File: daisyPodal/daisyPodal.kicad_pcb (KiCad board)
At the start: 2 copper layers, 76 x 82 mm, 50 parts, among them J1 Guitar in, J2 fsw pin 1, J3 fsw pin 2, J4 fsw pin 4, J5 fsw pin 5, J6 fsw pin 6, J7 Left out, J8 Right out, J9 fsw pin 3, SW1 Switch 1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

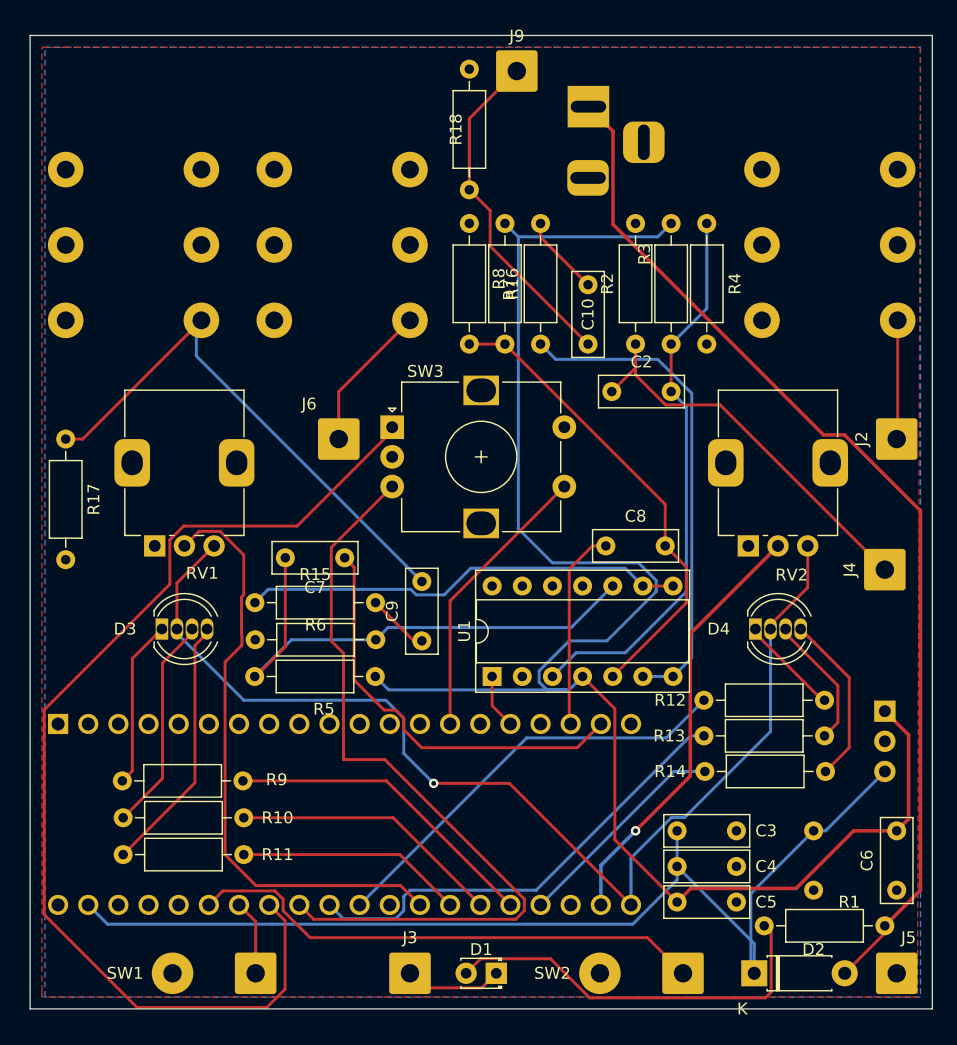
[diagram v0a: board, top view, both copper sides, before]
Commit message: Terminate unused op-amp
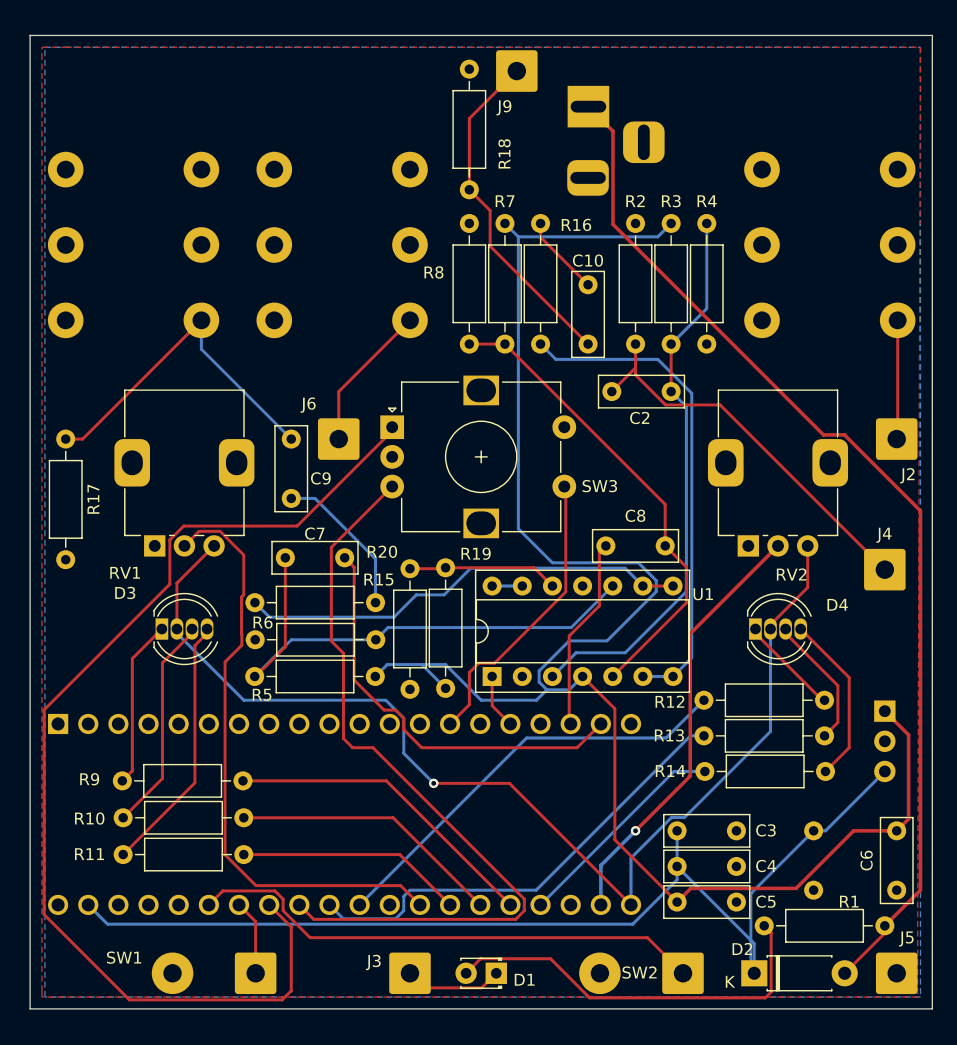
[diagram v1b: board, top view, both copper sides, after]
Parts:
- added R19: 1M, Resistor_THT:R_Axial_DIN0207_L6.3mm_D2.5mm_P10.16mm_Horizontal, F.Cu at (134.0, 107.0)
- added R20: 1M, Resistor_THT:R_Axial_DIN0207_L6.3mm_D2.5mm_P10.16mm_Horizontal, F.Cu at (131.0, 96.9)
- moved C9 16.3 mm to (121.0, 91.0)
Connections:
- U1 pad 12: (no net) -> Net-(U1D-+)
- U1 pad 13: (no net) -> Net-(U1D--)
- U1 pad 14: (no net) -> Net-(U1D--)
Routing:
- net Net-(C9-Pad2): track 45.9 -> 29.1 mm
- net Net-(U1D-+): track 0.00 -> 12.7 mm
- net Net-(C9-Pad1): track 5.24 -> 12.9 mm
- net Net-(U1D--): track 0.00 -> 2.54 mm
- net +5V: track 143.3 -> 145.8 mm
- net Net-(A1-SAI2_SD_B): track 66.4 -> 65.3 mm
- net /ENC_CLICK: track 24.0 -> 24.9 mm
- net /Left out: track 17.0 -> 16.3 mm
- net Net-(U1C--): track 37.4 -> 38.1 mm

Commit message: Add low pass filters at 22kHz on outputs
Following advice from Daisy forum discussion on Seed rev 7 noise.
Possible to jumper over these if not desired.
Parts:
- added C11: 2.2nF, Capacitor_THT:C_Rect_L7.0mm_W2.5mm_P5.00mm, F.Cu at (152.5, 91.8)
- added C12: 2.2nF, Capacitor_THT:C_Rect_L7.0mm_W2.5mm_P5.00mm, F.Cu at (102.0, 103.0)
- added R21: 3.3K, Resistor_THT:R_Axial_DIN0207_L6.3mm_D2.5mm_P10.16mm_Horizontal, F.Cu at (171.0, 106.1)
- added R22: 3.3K, Resistor_THT:R_Axial_DIN0207_L6.3mm_D2.5mm_P10.16mm_Horizontal, F.Cu at (112.1, 107.0)
- moved J4 5.04 mm to (171.6, 92.0)
- moved R17 1.16 mm to (102.0, 84.8)
- moved J2 0.49 mm to (171.5, 86.0)
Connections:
- C7 pad 1: /Right out -> Net-(C12-Pad2)
- C8 pad 1: /Left out -> Net-(C11-Pad2)
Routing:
- net Net-(C11-Pad2): track 0.00 -> 37.7 mm, vias 0 -> 1
- net Net-(C12-Pad2): track 0.00 -> 34.3 mm
- net /Left out: track 16.3 -> 33.7 mm
- net GND: track 0.00 -> 8.93 mm
- net Net-(BT1-+): track 88.3 -> 94.2 mm
- net /Right out: track 35.2 -> 38.4 mm, vias 0 -> 1
- net Net-(J4-Pin_1): track 35.2 -> 33.8 mm
- net Net-(A1-SAI2_SD_A): track 90.9 -> 91.5 mm

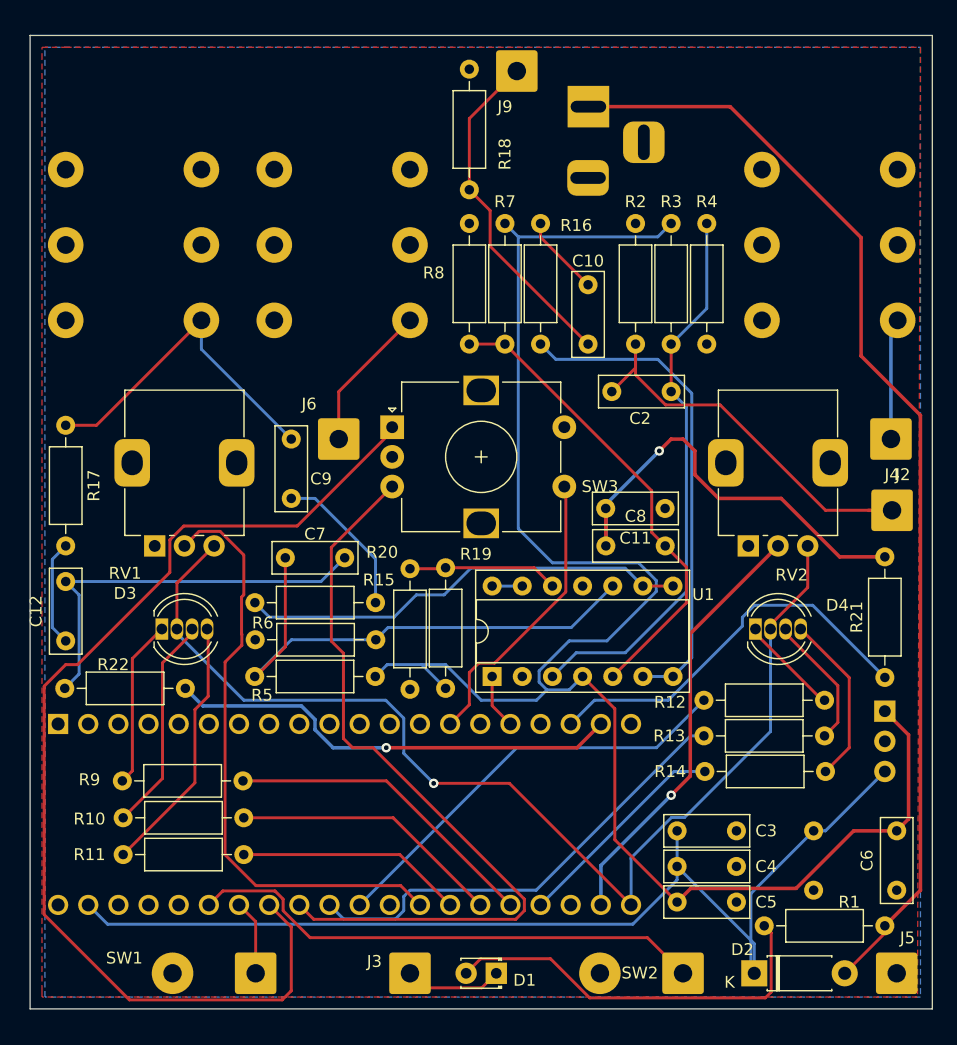
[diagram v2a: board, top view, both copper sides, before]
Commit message: Tidy up various overlaps
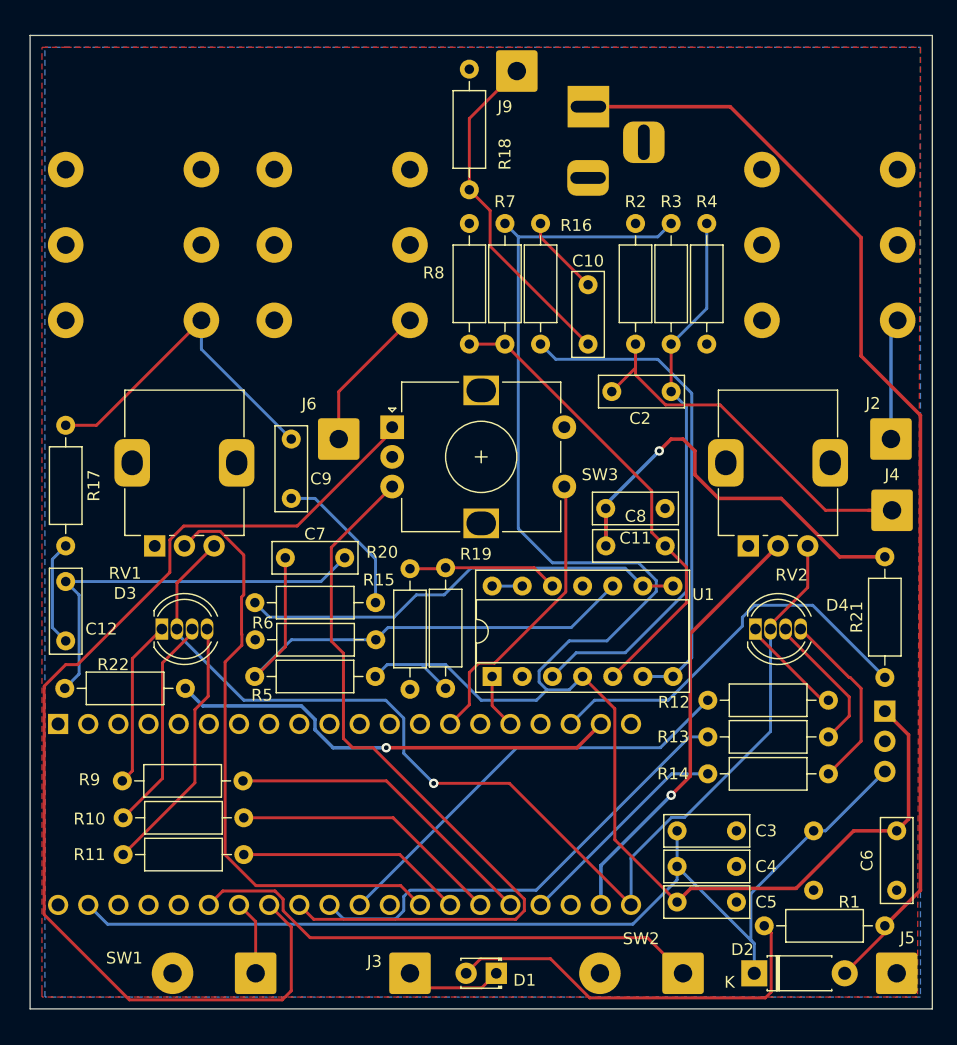
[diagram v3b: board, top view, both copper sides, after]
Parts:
- moved R13 0.34 mm to (156.1, 111.1)
- moved R12 0.33 mm to (156.1, 108.0)
- moved R14 0.32 mm to (156.1, 114.2)
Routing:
- net /VCC: track 90.0 -> 87.9 mm
- net Net-(D4-BK): track 14.5 -> 15.5 mm
- net Net-(D4-GK): track 11.3 -> 12.0 mm
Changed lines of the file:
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@@
   )
   (footprint "Resistor_THT:R_Axial_DIN0207_L6.3mm_D2.5mm_P10.16mm_Horizontal" (layer "F.Cu")
-    (at 155.76 111)
+    (at 156.087773 111.085472)
     (descr "Resistor, Axial_DIN0207 series, Axial, Horizontal, pin pitch=10.16mm, 0.25W = 1/4W, length*diameter=6.3*2.5mm^2, http://cdn-reichelt.de/documents/datenblatt/B400/1_4W%23YAG.pdf")
     (tags "Resistor Axial_DIN0207 series Axial Horizontal pin pitch 10.16mm 0.25W = 1/4W length 6.3mm diameter 2.5mm")
@@
     (property "ki_keywords" "connector")
     (attr exclude_from_pos_files)
-    (fp_text reference "J2" (at -3 1 180) (layer "F.SilkS")
+    (fp_text reference "J2" (at 2.995907 -1.514377 180) (layer "F.SilkS")
         (effects (font (size 1 1) (thickness 0.15)))
     )
@@
   )
   (footprint "Resistor_THT:R_Axial_DIN0207_L6.3mm_D2.5mm_P10.16mm_Horizontal" (layer "F.Cu")
-    (at 155.84 114)
+    (at 156.087773 114.197775)
     (descr "Resistor, Axial_DIN0207 series, Axial, Horizontal, pin pitch=10.16mm, 0.25W = 1/4W, length*diameter=6.3*2.5mm^2, http://cdn-reichelt.de/documents/datenblatt/B400/1_4W%23YAG.pdf")
     (tags "Resistor Axial_DIN0207 series Axial Horizontal pin pitch 10.16mm 0.25W = 1/4W length 6.3mm diameter 2.5mm")
@@
   )
   (footprint "Resistor_THT:R_Axial_DIN0207_L6.3mm_D2.5mm_P10.16mm_Horizontal" (layer "F.Cu")
-    (at 155.76 108)
+    (at 156.087773 108)
     (descr "Resistor, Axial_DIN0207 series, Axial, Horizontal, pin pitch=10.16mm, 0.25W = 1/4W, length*diameter=6.3*2.5mm^2, http://cdn-reichelt.de/documents/datenblatt/B400/1_4W%23YAG.pdf")
     (tags "Resistor Axial_DIN0207 series Axial Horizontal pin pitch 10.16mm 0.25W = 1/4W length 6.3mm diameter 2.5mm")
@@
     (property "ki_keywords" "rotary switch encoder switch push button")
     (attr through_hole)
-    (fp_text reference "SW3" (at 17.5 5) (layer "F.SilkS")
+    (fp_text reference "SW3" (at 17.5 4) (layer "F.SilkS")
         (effects (font (size 1 1) (thickness 0.15)))
     )
@@
     (property "ki_keywords" "cap capacitor")
     (attr through_hole)
-    (fp_text reference "C12" (at 2.5 -2.5 90) (layer "F.SilkS")
+    (fp_text reference "C12" (at 1 3 180) (layer "F.SilkS")
         (effects (font (size 1 1) (thickness 0.15)))
     )
@@
     (property "ki_keywords" "switch normally-open pushbutton push-button")
     (attr exclude_from_pos_files)
-    (fp_text reference "SW2" (at 3.640557 0.025561 180) (layer "F.SilkS")
+    (fp_text reference "SW2" (at 3.532001 2.913996 180) (layer "F.SilkS")
         (effects (font (size 1 1) (thickness 0.15)))
     )
@@
     (property "ki_keywords" "Voltage Regulator 100mA Positive")
     (attr through_hole)
-    (fp_text reference "U2" (at -2.92 0 90) (layer "B.SilkS")
+    (fp_text reference "U2" (at -1.451371 -2.306266 90) (layer "B.SilkS")
         (effects (font (size 1 1) (thickness 0.15)) (justify mirror))
     )
@@
   (gr_rect locked (start 99 52) (end 175 134)
     (stroke (width 0.1) (type default)) (fill none) (layer "Edge.Cuts"))
-  (gr_text "Podal v0.2 Denis Crowdy" (at 168 91 90) (layer "B.SilkS")
+  (gr_text "Podal v0.2 Denis Crowdy" (at 120.359779 112.923016) (layer "B.SilkS")
     (effects (font (size 1 1) (thickness 0.15)) (justify left bottom mirror))
   )
@@
   (segment (start 153 116) (end 147.08 121.92) (width 0.3) (layer "B.Cu") (net 22))
   (segment (start 147.08 121.92) (end 147.08 125.24) (width 0.3) (layer "B.Cu") (net 22))
-  (segment (start 155.84 114) (end 153.24 114) (width 0.25) (layer "B.Cu") (net 24))
-  (segment (start 153.24 114) (end 142 125.24) (width 0.25) (layer "B.Cu") (net 24))
+  (segment (start 153.042225 114.197775) (end 142 125.24) (width 0.25) (layer "B.Cu") (net 24))
+  (segment (start 156.087773 114.197775) (end 153.042225 114.197775) (width 0.25) (layer "B.Cu") (net 24))
   (segment (start 116.930684 114.791782) (end 129.011782 114.791782) (width 0.25) (layer "F.Cu") (net 25))
   (segment (start 129.011782 114.791782) (end 139.46 125.24) (width 0.25) (layer "F.Cu") (net 25))
@@
   (segment (start 112 95) (end 113.225 93.775) (width 0.25) (layer "F.Cu") (net 28))
   (segment (start 118.024009 123.615) (end 130.215 123.615) (width 0.25) (layer "F.Cu") (net 28))
-  (segment (start 155.76 108) (end 151.76 112) (width 0.25) (layer "B.Cu") (net 30))
-  (segment (start 151.76 112) (end 140 112) (width 0.25) (layer "B.Cu") (net 30))
-  (segment (start 140 112) (end 126.76 125.24) (width 0.25) (layer "B.Cu") (net 30))
+  (segment (start 152.087773 112) (end 156.087773 108) (width 0.25) (layer "B.Cu") (net 30))
+  (segment (start 140 112) (end 152.087773 112) (width 0.25) (layer "B.Cu") (net 30))
+  (segment (start 126.76 125.24) (end 140 112) (width 0.25) (layer "B.Cu") (net 30))
   (segment (start 130.475 125.726701) (end 129.786701 126.415) (width 0.25) (layer "B.Cu") (net 31))
-  (segment (start 155.76 111) (end 154.62863 111) (width 0.25) (layer "B.Cu") (net 31))
-  (segment (start 125.395 126.415) (end 124.22 125.24) (width 0.25) (layer "B.Cu") (net 31))
-  (segment (start 131 124) (end 130.475 124.525) (width 0.25) (layer "B.Cu") (net 31))
-  (segment (start 154.62863 111) (end 141.62863 124) (width 0.25) (layer "B.Cu") (net 31))
   (segment (start 141.62863 124) (end 131 124) (width 0.25) (layer "B.Cu") (net 31))
   (segment (start 129.786701 126.415) (end 125.395 126.415) (width 0.25) (layer "B.Cu") (net 31))
+  (segment (start 154.543158 111.085472) (end 141.62863 124) (width 0.25) (layer "B.Cu") (net 31))
+  (segment (start 156.087773 111.085472) (end 154.543158 111.085472) (width 0.25) (layer "B.Cu") (net 31))
   (segment (start 130.475 124.525) (end 130.475 125.726701) (width 0.25) (layer "B.Cu") (net 31))
+  (segment (start 131 124) (end 130.475 124.525) (width 0.25) (layer "B.Cu") (net 31))
+  (segment (start 125.395 126.415) (end 124.22 125.24) (width 0.25) (layer "B.Cu") (net 31))
   (segment (start 126.175 112) (end 127.881701 112) (width 0.25) (layer "F.Cu") (net 32))
   (segment (start 122.895305 126.455305) (end 121.68 125.24) (width 0.25) (layer "F.Cu") (net 32))
@@
   (segment (start 171 114) (end 166 119) (width 0.25) (layer "B.Cu") (net 39))
   (segment (start 153.5 123.13137) (end 149.76637 126.865) (width 0.25) (layer "B.Cu") (net 39))
+  (segment (start 159.715 128.215) (end 160 128.5) (width 0.25) (layer "B.Cu") (net 39))
+  (segment (start 159.715 124.285) (end 159.715 128.215) (width 0.25) (layer "B.Cu") (net 39))
   (segment (start 105.525 126.865) (end 103.9 125.24) (width 0.25) (layer "B.Cu") (net 39))
   (segment (start 149.76637 126.865) (end 105.525 126.865) (width 0.25) (layer "B.Cu") (net 39))
-  (segment (start 165 119) (end 159.715 124.285) (width 0.25) (layer "B.Cu") (net 39))
   (segment (start 153.5 122) (end 153.5 123.13137) (width 0.25) (layer "B.Cu") (net 39))
-  (segment (start 159.715 124.285) (end 159.715 130.715) (width 0.25) (layer "B.Cu") (net 39))
   (segment (start 153.5 122) (end 153.5 119) (width 0.25) (layer "B.Cu") (net 39))
+  (segment (start 165 119) (end 159.715 124.285) (width 0.25) (layer "B.Cu") (net 39))
   (segment (start 160 128.5) (end 153.5 122) (width 0.25) (layer "B.Cu") (net 39))
   (segment (start 159.715 130.715) (end 160 131) (width 0.25) (layer "B.Cu") (net 39))
@@
   (segment (start 112.885 108.785991) (end 112.885 114.955) (width 0.25) (layer "F.Cu") (net 49))
   (segment (start 160.1 102) (end 160.1 102.365) (width 0.25) (layer "F.Cu") (net 50))
+  (segment (start 165.735 108) (end 166.247773 108) (width 0.25) (layer "F.Cu") (net 50))
   (segment (start 160.1 102.365) (end 165.735 108) (width 0.25) (layer "F.Cu") (net 50))
-  (segment (start 165.735 108) (end 165.92 108) (width 0.25) (layer "F.Cu") (net 50))
-  (segment (start 167.045 109.875) (end 165.92 111) (width 0.25) (layer "F.Cu") (net 51))
-  (segment (start 167.045 106.77) (end 167.045 109.875) (width 0.25) (layer "F.Cu") (net 51))
-  (segment (start 162.64 102.365) (end 167.045 106.77) (width 0.25) (layer "F.Cu") (net 51))
-  (segment (start 162.64 102) (end 162.64 102.365) (width 0.25) (layer "F.Cu") (net 51))
+  (segment (start 168 107.725) (end 162.64 102.365) (width 0.25) (layer "F.Cu") (net 51))
+  (segment (start 168 109.333245) (end 168 107.725) (width 0.25) (layer "F.Cu") (net 51))
+  (segment (start 166.247773 111.085472) (end 168 109.333245) (width 0.25) (layer "F.Cu") (net 51))
+  (segment (start 162.64 102.365) (end 162.64 102) (width 0.25) (layer "F.Cu") (net 51))
+  (segment (start 169 111.445548) (end 166.247773 114.197775) (width 0.25) (layer "F.Cu") (net 52))
+  (segment (start 168 106.09) (end 168.09 106.09) (width 0.25) (layer "F.Cu") (net 52))
   (segment (start 163.91 102) (end 168 106.09) (width 0.25) (layer "F.Cu") (net 52))
-  (segment (start 168 106.09) (end 168 112) (width 0.25) (layer "F.Cu") (net 52))
-  (segment (start 168 112) (end 166 114) (width 0.25) (layer "F.Cu") (net 52))
+  (segment (start 168.09 106.09) (end 169 107) (width 0.25) (layer "F.Cu") (net 52))
+  (segment (start 169 107) (end 169 111.445548) (width 0.25) (layer "F.Cu") (net 52))
   (segment (start 172.081013 85.918987) (end 172 86) (width 0.25) (layer "F.Cu") (net 53))
   (segment (start 172 76) (end 171.514377 76.485623) (width 0.3) (layer "B.Cu") (net 53))
